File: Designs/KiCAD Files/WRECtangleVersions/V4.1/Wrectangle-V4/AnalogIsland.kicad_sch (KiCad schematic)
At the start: 5 parts, among them U12 ADS1256IDBRG4

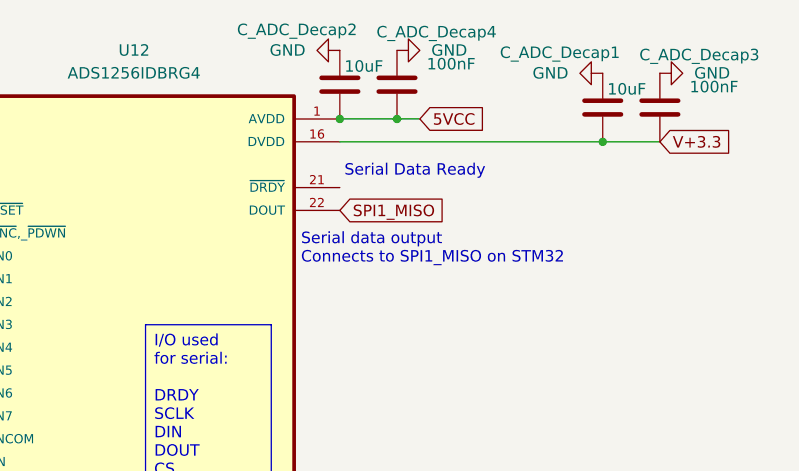
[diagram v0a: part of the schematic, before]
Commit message: made some minor fixes to pins
Added DRDY to ADC
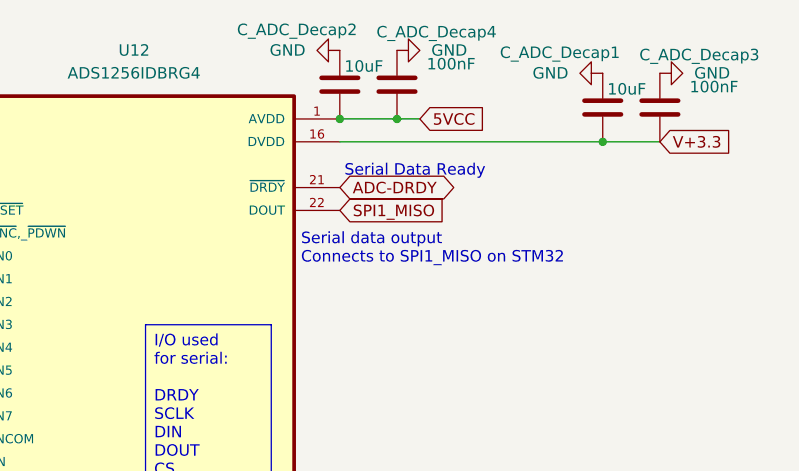
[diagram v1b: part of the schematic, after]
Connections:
- net ADC-DRDY: now reaches U12.21 (~{DRDY})
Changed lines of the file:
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@@
+		)
+	)
+	(global_label "ADC-DRDY"
+		(shape bidirectional)
+		(at 165.1 76.2 0)
+		(fields_autoplaced yes)
+		(effects
+			(font
+				(size 1.27 1.27)
+			)
+			(justify left)
+		)
+		(property "Intersheetrefs" "${INTERSHEET_REFS}"
+			(at 179.2961 76.2 0)
+			(effects
+				(font
+					(size 1.27 1.27)
+				)
+				(justify left)
+				(hide yes)
+			)
 		)
 	)
